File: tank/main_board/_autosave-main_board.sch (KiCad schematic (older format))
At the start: 35 parts, among them J1 PowerIn, J10 Sonar2, J11 Programming Header, J12 SigOut, J16 PowerOut, J2 M2, J3 M1, J4 LEDs, J5 M3, J6 Spk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

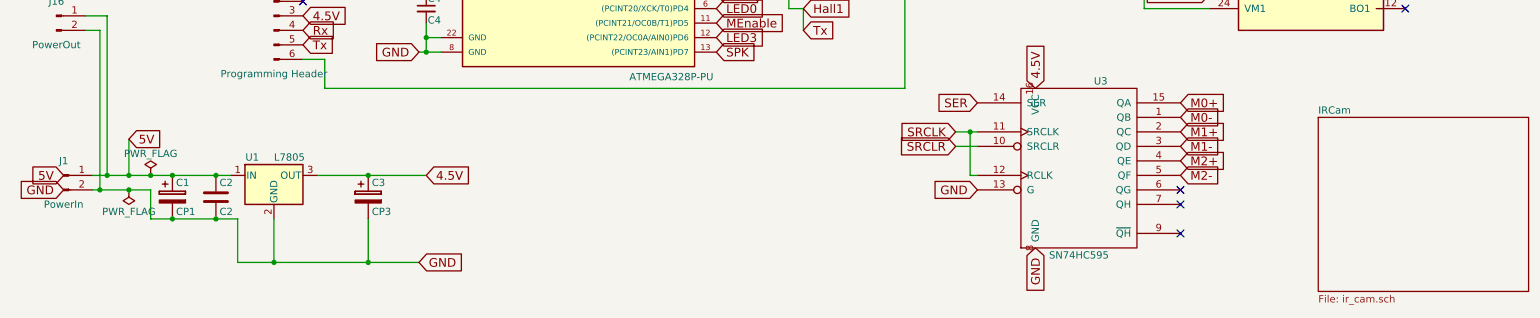
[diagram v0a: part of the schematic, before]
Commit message: migrate to KiCad 5.1.5
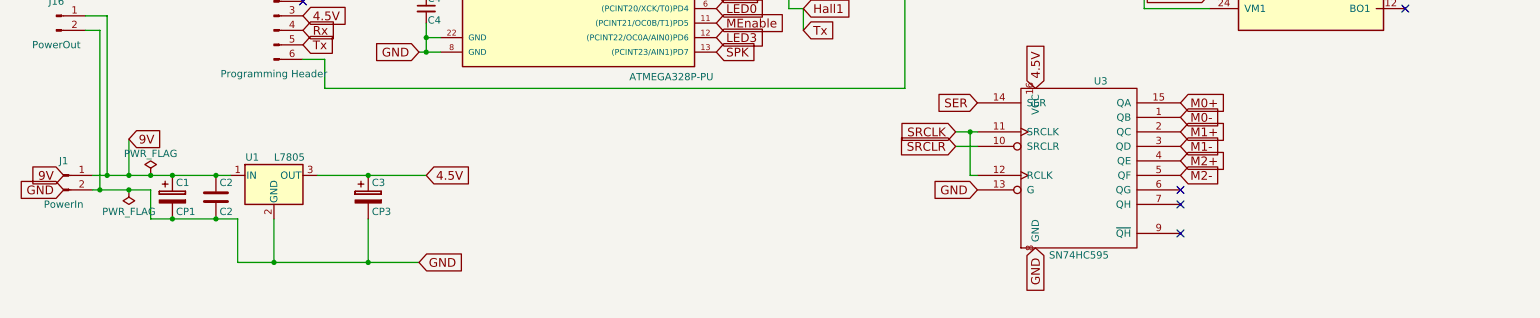
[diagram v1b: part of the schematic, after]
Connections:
- net 5V: no longer C1.1, C2.1, J1.1 (Pin_1), J16.1 (Pin_1), U1.1 (IN)
- new net 9V: C1.1, C2.1, J1.1 (Pin_1), J16.1 (Pin_1), U1.1 (IN)
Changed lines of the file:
@@
 $Descr A4 11693 8268
 encoding utf-8
-Sheet 1 2
+Sheet 1 1
 Title ""
 Date ""
@@
 GND
 Text GLabel 1200 5300 2    60   Input ~ 0
-5V
+9V
 Text GLabel 750  5550 0    60   Input ~ 0
-5V
+9V
 Text GLabel 750  5650 0    60   Input ~ 0
 GND
@@
 Wire Wire Line
 	1000 5650 1200 5650
-$Sheet
-S 9400 5150 1450 1200
-U 5E87C6BA
-F0 "IRCam" 50
-F1 "ir_cam.sch" 50
-$EndSheet
 Wire Wire Line
 	5850 4400 5850 4550
